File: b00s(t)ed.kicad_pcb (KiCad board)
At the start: 2 copper layers, 21 x 19 mm, 10 parts, among them Q1 IRF7739L1, Q2 2N7002W, U1 LM5050-2, U2 NSI50010YT1G

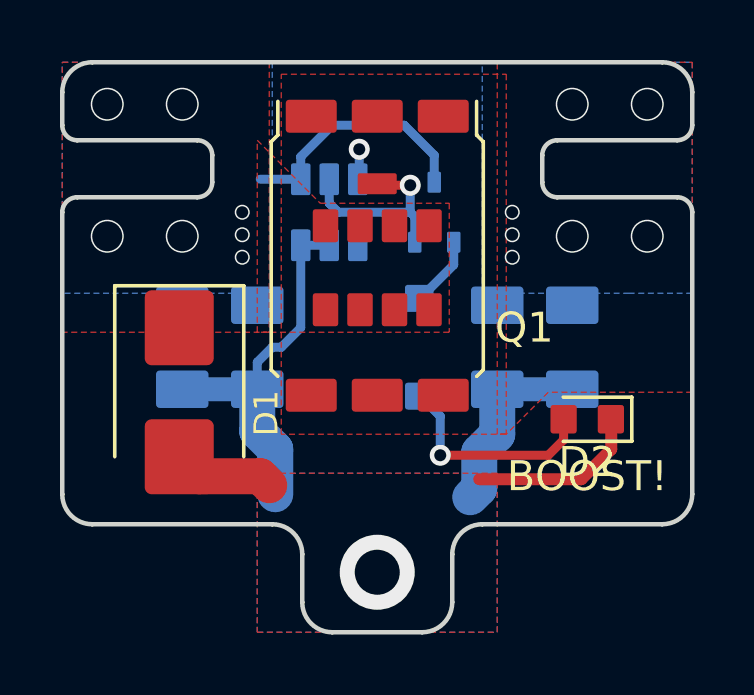
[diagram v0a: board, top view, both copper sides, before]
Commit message: Switch over to LM5050-1
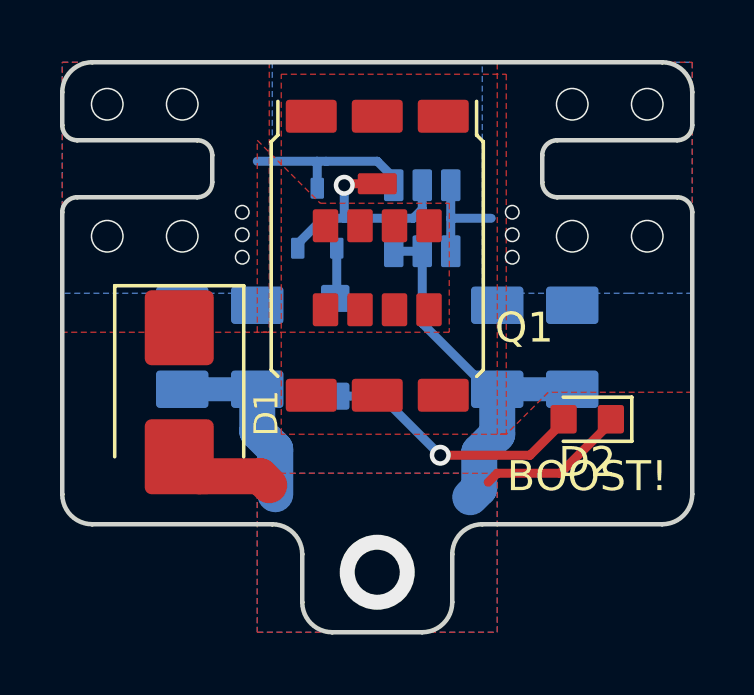
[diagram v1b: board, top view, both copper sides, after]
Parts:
- U1: value LM5050-2 -> LM5050-1
- moved Q2 3.91 mm to (138.0, 65.2)
- moved U1 3.11 mm to (141.5, 65.2)
- moved U2 2.80 mm to (138.6, 69.5)
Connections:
- U1 pad 1: (no net) -> /OUT
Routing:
- net /OUT: track 1.02 -> 3.55 mm, vias 8 -> 7
- net +BATT: track 8.30 -> 5.93 mm
- net Net-(D2-Pad2): track 7.41 -> 9.08 mm
- net Net-(Q1-Pad2): track 6.71 -> 7.80 mm
- net Net-(Q2-Pad1): track 2.38 -> 1.69 mm
- net -BATT: track 28.3 -> 27.7 mm
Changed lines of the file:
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@@
     (thickness 0.8)
     (drawings 43)
-    (tracks 63)
+    (tracks 62)
     (zones 0)
     (modules 10)
@@
   )
   (module Package_TO_SOT_SMD:SOT-23-6 (layer B.Cu)
-    (at 138.4 65 90)
+    (at 141.5 65.2 90)
     (descr "6-pin SOT-23 package")
     (tags SOT-23-6)
@@
       (effects (font (size 1 1) (thickness 0.15)) (justify mirror))
     )
-    (fp_text value LM5050-2 (at 0 -2.9 90) (layer B.Fab)
+    (fp_text value LM5050-1 (at 0 -2.9 90) (layer B.Fab)
       (effects (font (size 1 1) (thickness 0.15)) (justify mirror))
     )
@@
     (pad 2 smd roundrect (at -1.1 0 90) (size 1.06 0.65) (layers B.Cu B.Paste B.Mask) (roundrect_rratio 0.1)
       (net 3 -BATT))
-    (pad 1 smd roundrect (at -1.1 0.95 90) (size 1.06 0.65) (layers B.Cu B.Paste B.Mask) (roundrect_rratio 0.1))
+    (pad 1 smd roundrect (at -1.1 0.95 90) (size 1.06 0.65) (layers B.Cu B.Paste B.Mask) (roundrect_rratio 0.1)
+      (net 2 /OUT))
     (model ${KISYS3DMOD}/Package_TO_SOT_SMD.3dshapes/SOT-23-6.wrl
       (at (xyz 0 0 0))
@@
   )
   (module Package_TO_SOT_SMD:SOT-323_SC-70 (layer B.Cu)
-    (at 141.9 65 90)
+    (at 138 65.2 90)
     (descr "SOT-323, SC-70")
     (tags "SOT-323 SC-70")
@@
   )
   (module Digikey:SOD-123 (layer B.Cu)
-    (at 141.4 69.5 90)
+    (at 138.6 69.5 90)
     (fp_text reference U2 (at -0.01 1.89 90) (layer B.SilkS) hide
       (effects (font (size 1 1) (thickness 0.15)) (justify mirror))
@@
   (gr_line (start 130.5 60) (end 149.5 60) (layer Edge.Cuts) (width 0.15))
   (gr_line (start 134.5 64) (end 134.5 63.1) (layer Edge.Cuts) (width 0.15))
-  (via (at 141.1 64.1) (size 0.7) (drill 0.4) (layers F.Cu B.Cu) (net 1))
-  (segment (start 140.05 64.1) (end 140 64.05) (width 0.3) (layer F.Cu) (net 1))
-  (segment (start 141.1 64.1) (end 140.05 64.1) (width 0.3) (layer F.Cu) (net 1))
-  (segment (start 138.4 64.7) (end 138.7 65) (width 0.3) (layer B.Cu) (net 1))
-  (segment (start 138.4 63.9) (end 138.4 64.7) (width 0.3) (layer B.Cu) (net 1))
-  (segment (start 138.7 65) (end 141.1 65) (width 0.3) (layer B.Cu) (net 1))
-  (segment (start 141.1 65) (end 141.1 64.1) (width 0.3) (layer B.Cu) (net 1))
-  (segment (start 141.25 65.15) (end 141.25 66) (width 0.3) (layer B.Cu) (net 1))
-  (segment (start 141.1 65) (end 141.25 65.15) (width 0.3) (layer B.Cu) (net 1))
+  (via (at 138.9 64.1) (size 0.7) (drill 0.4) (layers F.Cu B.Cu) (net 1))
+  (segment (start 138.95 64.05) (end 140 64.05) (width 0.3) (layer F.Cu) (net 1))
+  (segment (start 138.9 64.1) (end 138.95 64.05) (width 0.3) (layer F.Cu) (net 1))
+  (segment (start 138.9 65.2) (end 138.9 64.1) (width 0.3) (layer B.Cu) (net 1))
+  (segment (start 138.2 65.2) (end 138.9 65.2) (width 0.3) (layer B.Cu) (net 1))
+  (segment (start 137.35 66.05) (end 138.2 65.2) (width 0.3) (layer B.Cu) (net 1))
+  (segment (start 137.35 66.2) (end 137.35 66.05) (width 0.3) (layer B.Cu) (net 1))
+  (segment (start 141.2 65.2) (end 138.9 65.2) (width 0.3) (layer B.Cu) (net 1))
+  (segment (start 141.5 64.9) (end 141.2 65.2) (width 0.3) (layer B.Cu) (net 1))
+  (segment (start 141.5 64.1) (end 141.5 64.9) (width 0.3) (layer B.Cu) (net 1))
   (via (at 149 61.4) (size 1.1) (drill 1) (layers F.Cu B.Cu) (net 2))
   (via (at 146.5 61.4) (size 1.1) (drill 1) (layers F.Cu B.Cu) (net 2))
@@
   (via (at 144.5 65.75) (size 0.5) (drill 0.4) (layers F.Cu B.Cu) (net 2))
   (via (at 144.5 66.5) (size 0.5) (drill 0.4) (layers F.Cu B.Cu) (net 2))
-  (via (at 139.4 62.9) (size 0.7) (drill 0.4) (layers F.Cu B.Cu) (net 2))
-  (segment (start 139.4 63.85) (end 139.35 63.9) (width 0.3) (layer B.Cu) (net 2))
-  (segment (start 139.4 62.9) (end 139.4 63.85) (width 0.3) (layer B.Cu) (net 2))
+  (segment (start 142.45 64.1) (end 142.45 65.2) (width 0.3) (layer B.Cu) (net 2))
+  (segment (start 142.45 65.2) (end 143.8 65.2) (width 0.3) (layer B.Cu) (net 2))
+  (segment (start 142.45 65.2) (end 142.45 66.3) (width 0.3) (layer B.Cu) (net 2))
   (via (at 140 77) (size 2.5) (drill 1.5) (layers F.Cu B.Cu) (net 3))
   (segment (start 136.1 73.8) (end 136.4 74.1) (width 1.2) (layer F.Cu) (net 3))
   (segment (start 134.05 73.8) (end 136.1 73.8) (width 1.2) (layer F.Cu) (net 3))
   (segment (start 133.4 73.15) (end 134.05 73.8) (width 1.2) (layer F.Cu) (net 3))
-  (segment (start 136 70) (end 136 70.9) (width 0.3) (layer B.Cu) (net 3))
-  (segment (start 136.8 69.5) (end 136.5 69.5) (width 0.3) (layer B.Cu) (net 3))
-  (segment (start 137.45 68.85) (end 136.8 69.5) (width 0.3) (layer B.Cu) (net 3))
-  (segment (start 136.5 69.5) (end 136 70) (width 0.3) (layer B.Cu) (net 3))
   (segment (start 136.6 72.9) (end 136.6 74.4) (width 1.2) (layer B.Cu) (net 3))
   (segment (start 136 72.3) (end 136.6 72.9) (width 1.2) (layer B.Cu) (net 3))
@@
   (segment (start 144 72.4) (end 143.4 73) (width 1.2) (layer B.Cu) (net 3))
   (segment (start 144 70.9) (end 144 72.4) (width 1.2) (layer B.Cu) (net 3))
-  (segment (start 137.45 68.85) (end 137.45 66.1) (width 0.3) (layer B.Cu) (net 3))
-  (segment (start 138.4 66.1) (end 137.45 66.1) (width 0.3) (layer B.Cu) (net 3))
-  (segment (start 147.8 72.9) (end 147.8 72) (width 0.4) (layer F.Cu) (net 3))
-  (segment (start 146.8 73.9) (end 147.8 72.9) (width 0.4) (layer F.Cu) (net 3))
-  (segment (start 143.4 73.9) (end 146.8 73.9) (width 0.4) (layer F.Cu) (net 3))
   (segment (start 146.5 70.9) (end 144 70.9) (width 0.8) (layer B.Cu) (net 3))
   (segment (start 136 70.9) (end 133.5 70.9) (width 0.8) (layer B.Cu) (net 3))
+  (segment (start 140.55 66.3) (end 141.5 66.3) (width 0.3) (layer B.Cu) (net 3))
+  (segment (start 143.7 70.9) (end 144 70.9) (width 0.3) (layer B.Cu) (net 3))
+  (segment (start 141.5 68.7) (end 143.7 70.9) (width 0.3) (layer B.Cu) (net 3))
+  (segment (start 141.5 66.3) (end 141.5 68.7) (width 0.3) (layer B.Cu) (net 3))
+  (segment (start 146.1 73.7) (end 147.8 72) (width 0.3) (layer F.Cu) (net 3))
+  (segment (start 144 73.7) (end 146.1 73.7) (width 0.3) (layer F.Cu) (net 3))
+  (segment (start 143.7 74) (end 144 73.7) (width 0.3) (layer F.Cu) (net 3))
   (via (at 133.5 61.4) (size 1.1) (drill 1) (layers F.Cu B.Cu) (net 4))
   (via (at 135.5 66.5) (size 0.5) (drill 0.4) (layers F.Cu B.Cu) (net 4))
@@
   (via (at 131 61.4) (size 1.1) (drill 1) (layers F.Cu B.Cu) (net 4))
   (via (at 131 65.8) (size 1.1) (drill 1) (layers F.Cu B.Cu) (net 4))
-  (segment (start 137.45 63.9) (end 136.1 63.9) (width 0.3) (layer B.Cu) (net 4))
-  (segment (start 138.5 62.1) (end 137.45 63.15) (width 0.3) (layer B.Cu) (net 4))
-  (segment (start 140.9 62.1) (end 138.5 62.1) (width 0.3) (layer B.Cu) (net 4))
-  (segment (start 137.45 63.15) (end 137.45 63.9) (width 0.3) (layer B.Cu) (net 4))
-  (segment (start 141.9 63.1) (end 140.9 62.1) (width 0.3) (layer B.Cu) (net 4))
-  (segment (start 141.9 64) (end 141.9 63.1) (width 0.3) (layer B.Cu) (net 4))
+  (segment (start 140 63.3) (end 138.3 63.3) (width 0.3) (layer B.Cu) (net 4))
+  (segment (start 140.55 63.85) (end 140 63.3) (width 0.3) (layer B.Cu) (net 4))
+  (segment (start 140.55 64.1) (end 140.55 63.85) (width 0.3) (layer B.Cu) (net 4))
+  (segment (start 138 64.2) (end 138 63.3) (width 0.3) (layer B.Cu) (net 4))
+  (segment (start 138 63.3) (end 136 63.3) (width 0.3) (layer B.Cu) (net 4))
+  (segment (start 138.3 63.3) (end 138 63.3) (width 0.3) (layer B.Cu) (net 4))
   (segment (start 146.325 71.9) (end 146.2125 71.9) (width 0.3) (layer F.Cu) (net 5))
   (via (at 142.1 73.1) (size 0.7) (drill 0.4) (layers F.Cu B.Cu) (net 5))
-  (segment (start 145.7 73.1) (end 146.2125 72.5875) (width 0.3) (layer F.Cu) (net 5))
-  (segment (start 146.2125 72.5875) (end 146.2125 71.9) (width 0.3) (layer F.Cu) (net 5))
-  (segment (start 142.1 73.1) (end 145.7 73.1) (width 0.3) (layer F.Cu) (net 5))
-  (segment (start 142.1 71.8) (end 142.1 73.1) (width 0.3) (layer B.Cu) (net 5))
-  (segment (start 141.4 71.1) (end 142.1 71.8) (width 0.3) (layer B.Cu) (net 5))
-  (segment (start 142.55 66.75) (end 142.55 66) (width 0.3) (layer B.Cu) (net 6))
-  (segment (start 141.4 67.9) (end 142.55 66.75) (width 0.3) (layer B.Cu) (net 6))
+  (segment (start 138.6 71.13) (end 140.13 71.13) (width 0.3) (layer B.Cu) (net 5))
+  (segment (start 140.13 71.13) (end 142.1 73.1) (width 0.3) (layer B.Cu) (net 5))
+  (segment (start 146.2125 71.979656) (end 146.2125 71.9) (width 0.3) (layer F.Cu) (net 5))
+  (segment (start 145.092156 73.1) (end 146.2125 71.979656) (width 0.3) (layer F.Cu) (net 5))
+  (segment (start 142.1 73.1) (end 145.092156 73.1) (width 0.3) (layer F.Cu) (net 5))
+  (segment (start 138.65 67.82) (end 138.6 67.87) (width 0.3) (layer B.Cu) (net 6))
+  (segment (start 138.65 66.2) (end 138.65 67.82) (width 0.3) (layer B.Cu) (net 6))
   (zone (net 4) (net_name +BATT) (layer F.Cu) (hatch edge 0.508)
     (priority 2)

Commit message: Date update
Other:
- board text added: "2019-02-12"
- board text removed: "2019-02-11"
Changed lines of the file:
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@@
   )
   (gr_poly (pts (xy 144.2 60) (xy 150.5 60) (xy 150.5 67) (xy 144.2 67)) (layer F.Mask) (width 0.15))
-  (gr_text 2019-02-11 (at 140 62.5) (layer B.SilkS)
+  (gr_text 2019-02-12 (at 140 62.5) (layer B.SilkS)
     (effects (font (size 0.8128 0.8) (thickness 0.153)) (justify mirror))
   )
